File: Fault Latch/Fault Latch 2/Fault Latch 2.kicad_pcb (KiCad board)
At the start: 2 copper layers, 85 x 85 mm, 108 parts, among them J1 1053141312, J3 1053131202, J4 1053131202, K101 Fujitsu_FTR-LYAA005x, K102 Fujitsu_FTR-LYAA005x, K103 Fujitsu_FTR-LYAA005x, Q101 Q_NPN_BEC, Q102 Q_NPN_BEC, Q103 Q_NPN_BEC, Q104 Q_NPN_BEC, Q105 Q_NMOS_GSD, Q106 Q_NMOS_GSD, Q107 Q_PMOS_GSD, Q108 Q_PMOS_GSD, Q109 Q_PMOS_GSD, Q110 Q_NPN_BEC, Q111 Q_NPN_BEC, Q112 Q_NMOS_GSD, Q113 Q_NMOS_GSD, Q114 Q_NMOS_GSD, Q115 Q_NMOS_GSD, Q116 Q_NMOS_GSD, SW101 SW_Omron_B3FS, SW102 SW_Omron_B3FS, SW103 SW_Omron_B3FS, U101 SFH617A-1, U102 SFH617A-1, U103 SFH617A-1, U104 74AHC1G00, U105 74AHC1G00, U106 74AHC1G00, U107 74LS279, U109 SFH617A-1, U110 SFH617A-1, U117 74AHC1G00, U118 LM555xM, U119 74AHC1G00, U121 SFH617A-1, U2 LM1117DT-5.0

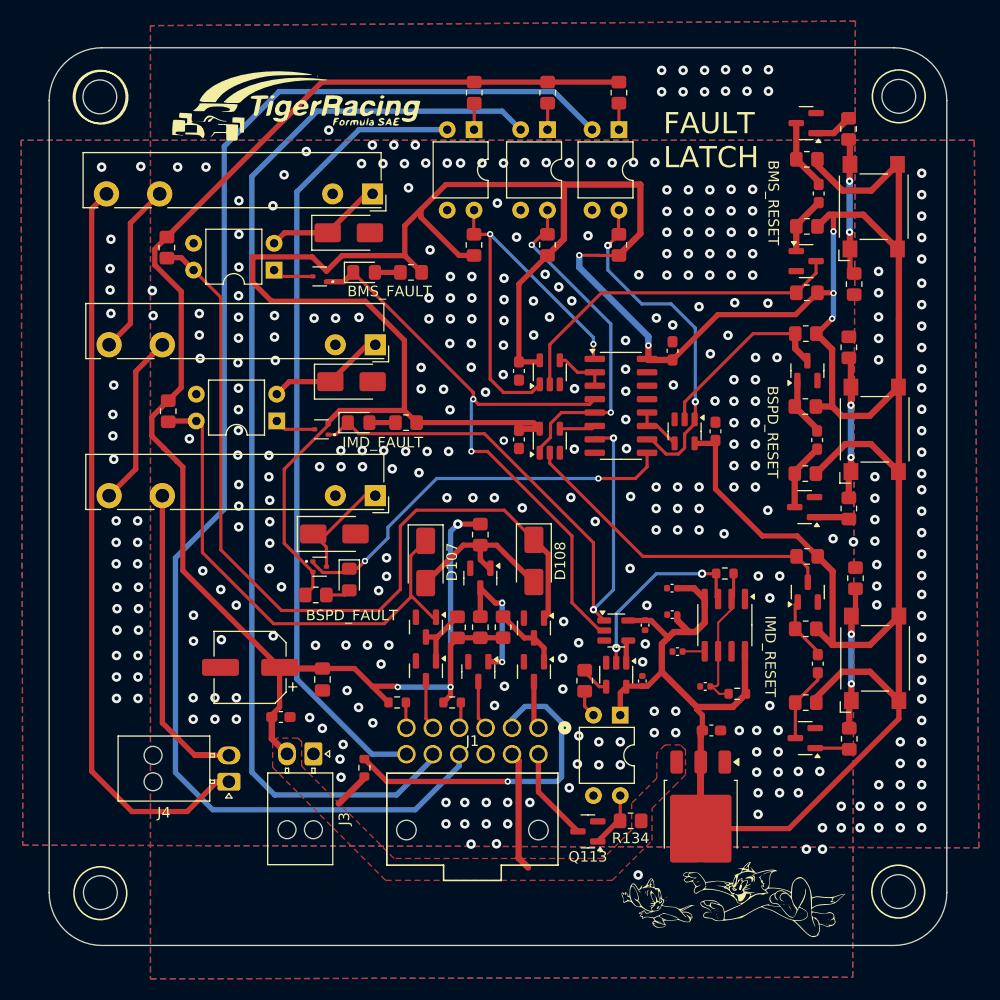
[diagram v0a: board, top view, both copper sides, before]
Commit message: Added Measuring points to Fault Latch
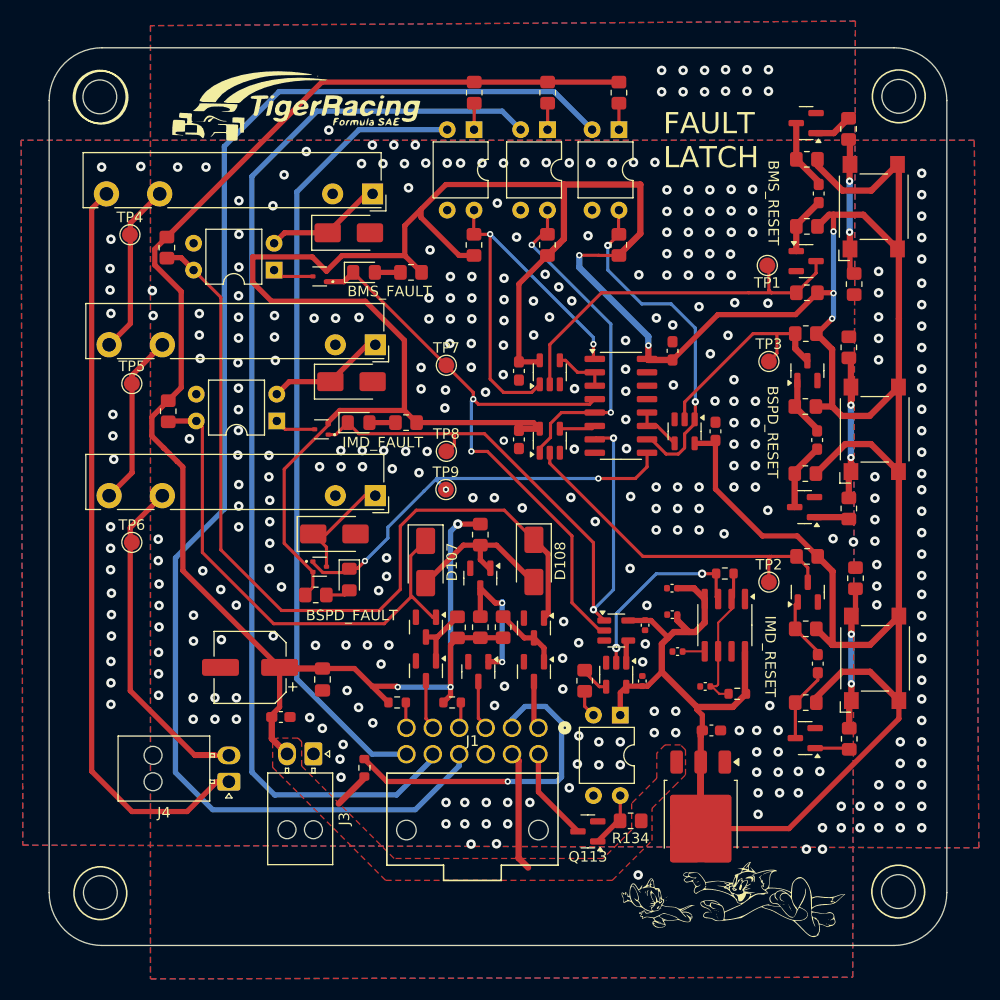
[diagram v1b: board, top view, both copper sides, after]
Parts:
- added TP1: TestPoint_BMS, TestPoint:TestPoint_Pad_D1.5mm, F.Cu at (137.3, 65.0)
- added TP2: TestPoint_IMD, TestPoint:TestPoint_Pad_D1.5mm, F.Cu at (137.4, 95.0)
- added TP3: TestPoint_BSPD, TestPoint:TestPoint_Pad_D1.5mm, F.Cu at (137.4, 74.1)
- added TP4: TestPoint_BMS_Shutdown, TestPoint:TestPoint_Pad_D1.5mm, F.Cu at (76.9, 62.1)
- added TP5: TestPoint_IMD_Shutdown, TestPoint:TestPoint_Pad_D1.5mm, F.Cu at (77.1, 76.2)
- added TP6: TestPoint_BSPD_Shutdown, TestPoint:TestPoint_Pad_D1.5mm, F.Cu at (77.1, 91.2)
- added TP7: TestPoint_SR_BMS, TestPoint:TestPoint_Pad_D1.5mm, F.Cu at (106.9, 74.4)
- added TP8: TestPoint_SR_IMD, TestPoint:TestPoint_Pad_D1.5mm, F.Cu at (106.9, 82.6)
- added TP9: TestPoint_SR_BSPD, TestPoint:TestPoint_Pad_D1.5mm, F.Cu at (106.9, 86.2)
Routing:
- net /NRESET_BSPD: track 17.8 -> 20.8 mm
- net /NRESET_BMS: track 32.9 -> 35.7 mm
- net /NRESET_IMD: track 30.9 -> 33.5 mm
- net /Shutdown Circuit Out: track 31.0 -> 33.5 mm
- net /IMD_SR: track 56.9 -> 58.9 mm
- net Net-(D103-K): track 38.2 -> 39.6 mm, vias 2 -> 3
- net GND: vias 355 -> 343

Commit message: Fault Latch Spring Semester
Fixed TSSI, Logic, and everything.
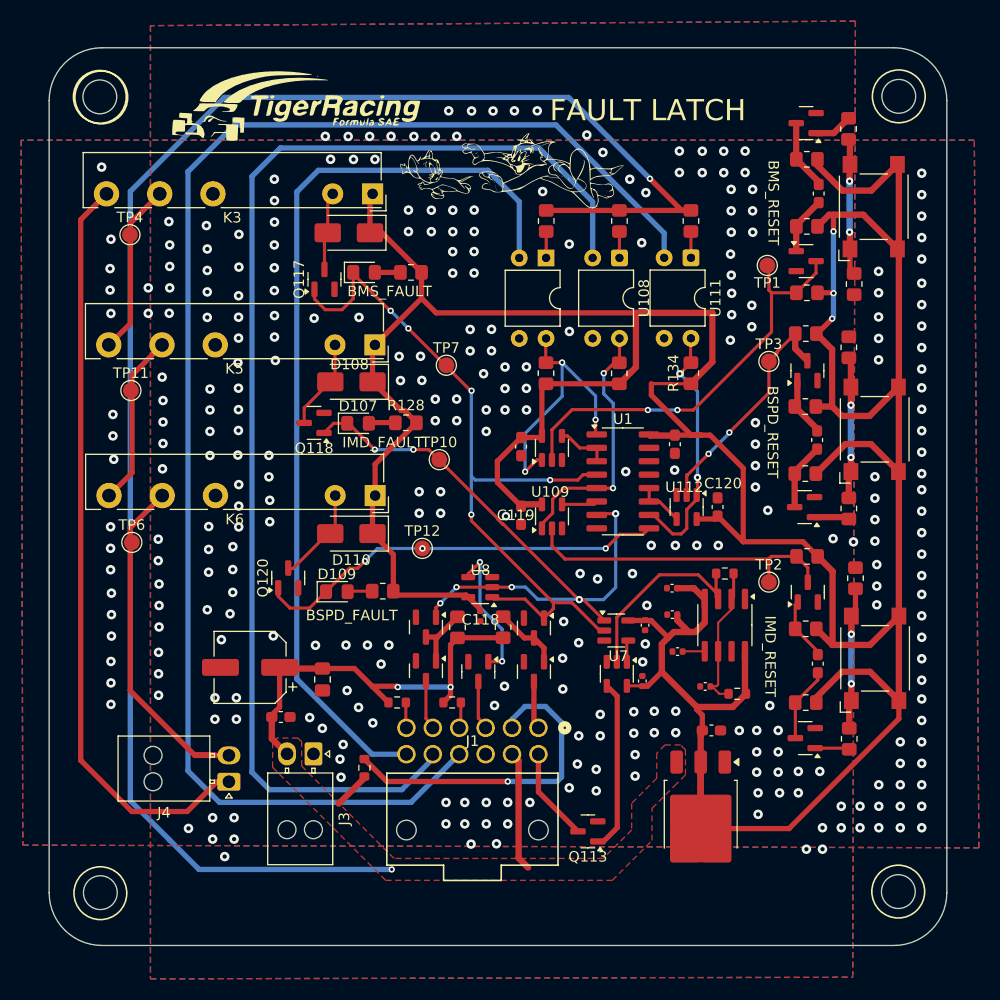
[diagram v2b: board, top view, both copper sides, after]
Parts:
- removed C103, C104: 100n, Capacitor_SMD:C_0603_1608Metric_Pad1.08x0.95mm_HandSolder
- removed D101, D103: RED, LED_SMD:LED_0805_2012Metric_Pad1.15x1.40mm_HandSolder
- removed D105, D106: D_Schottky, Diode_SMD:D_SMA
- removed K101, K102, K103: Fujitsu_FTR-LYAA005x, Relay_THT:Relay_SPST-NO_Fujitsu_FTR-LYAA005x_FormA_Vertical
- removed Q107, Q108, Q109: Q_PMOS_GSD, Package_TO_SOT_SMD:SOT-523
- removed Q116: Q_NMOS_GSD, Package_TO_SOT_SMD:SOT-23
- removed R103, R104: 220, Resistor_SMD:R_0805_2012Metric_Pad1.20x1.40mm_HandSolder
- removed R107, R109: 1k, Resistor_SMD:R_0805_2012Metric_Pad1.20x1.40mm_HandSolder
- removed R116, R118: 2k, Resistor_SMD:R_0805_2012Metric_Pad1.20x1.40mm_HandSolder
- removed R138: 10k, Resistor_SMD:R_0805_2012Metric_Pad1.20x1.40mm_HandSolder
- removed TP5: TestPoint_IMD_Shutdown, TestPoint:TestPoint_Pad_D1.5mm
- removed TP8: TestPoint_SR_IMD, TestPoint:TestPoint_Pad_D1.5mm
- removed TP9: TestPoint_SR_BSPD, TestPoint:TestPoint_Pad_D1.5mm
- removed U102, U103, U110, U121: SFH617A-1, Package_DIP:DIP-4_W7.62mm
- removed U105, U106, U119: 74AHC1G00, Package_TO_SOT_SMD:SOT-23-5
- removed U107: 74LS279, Package_SO:SOIC-16_3.9x9.9mm_P1.27mm
- added C118: 0.1u, Capacitor_SMD:C_0402_1005Metric, F.Cu at (110.1, 98.2)
- added C119: 100n, Capacitor_SMD:C_0603_1608Metric_Pad1.08x0.95mm_HandSolder, F.Cu at (114.0, 88.6)
- added C120: 100n, Capacitor_SMD:C_0603_1608Metric_Pad1.08x0.95mm_HandSolder, F.Cu at (132.6, 87.9)
- added D109: RED, LED_SMD:LED_0805_2012Metric_Pad1.15x1.40mm_HandSolder, F.Cu at (96.5, 95.9)
- added D110: D_Schottky, Diode_SMD:D_SMA, F.Cu at (97.9, 90.4)
- added K3: Fujitsu_FTR-LYCA005x, Relay_THT:Relay_SPDT_Fujitsu_FTR-LYCA005x_FormC_Vertical, F.Cu at (99.9, 58.2)
- added K5: Fujitsu_FTR-LYCA005x, Relay_THT:Relay_SPDT_Fujitsu_FTR-LYCA005x_FormC_Vertical, F.Cu at (100.1, 72.5)
- added K6: Fujitsu_FTR-LYCA005x, Relay_THT:Relay_SPDT_Fujitsu_FTR-LYCA005x_FormC_Vertical, F.Cu at (100.1, 86.8)
- added Q117: Q_NMOS_GSD, Package_TO_SOT_SMD:SOT-23, F.Cu at (95.4, 66.3)
- added Q118: Q_NMOS_GSD, Package_TO_SOT_SMD:SOT-23, F.Cu at (94.4, 79.9)
- added Q120: Q_NMOS_GSD, Package_TO_SOT_SMD:SOT-23, F.Cu at (91.9, 94.6)
- added R128: 2k, Resistor_SMD:R_0805_2012Metric_Pad1.20x1.40mm_HandSolder, F.Cu at (103.1, 79.9)
- added TP10: TestPoint_SR_IMD, TestPoint:TestPoint_Pad_D1.5mm, F.Cu at (106.2, 83.4)
- added TP11: TestPoint_IMD_Shutdown, TestPoint:TestPoint_Pad_D1.5mm, F.Cu at (77.0, 76.8)
- added TP12: TestPoint_SR_BSPD, TestPoint:TestPoint_Pad_D1.5mm, F.Cu at (104.6, 91.8)
- added U1: 74LS279, Package_SO:SOIC-16_3.9x9.9mm_P1.27mm, F.Cu at (123.6, 85.4)
- added U108: SFH617A-1, Package_DIP:DIP-4_W7.62mm, F.Cu at (123.3, 64.3)
- added U111: SFH617A-1, Package_DIP:DIP-4_W7.62mm, F.Cu at (130.1, 64.3)
- added U112: 74AHC1G00, Package_TO_SOT_SMD:SOT-23-5, F.Cu at (129.6, 87.9)
- added U7: SN74AHC1G08DBVR, Package_TO_SOT_SMD:SOT-23-5, F.Cu at (123.0, 103.7)
- added U8: SN74AHC1G08DBVR, Package_TO_SOT_SMD:SOT-23-5, F.Cu at (110.1, 95.4)
- D107: value D_Schottky -> RED; footprint Diode_SMD:D_SMA -> LED_SMD:LED_0805_2012Metric_Pad1.15x1.40mm_HandSolder
- R125: value 10k -> 220
- R126, R134: value 10k -> 1k
- R137: value 10k -> 2k
- U109: value SFH617A-1 -> 74AHC1G00; footprint Package_DIP:DIP-4_W7.62mm -> Package_TO_SOT_SMD:SOT-23-5
- moved G*** 72.1 mm to (112.3, 55.9)
- moved R133 44.7 mm to (130.1, 60.8)
- moved R125 42.9 mm to (123.3, 60.8), turned to 90 degrees
- moved R126 42.9 mm to (123.3, 75.2), turned to 90 degrees
- moved R134 42.8 mm to (130.1, 75.2), turned to 90 degrees
- moved U109 35.2 mm to (116.9, 88.7), turned to 90 degrees
- moved D108 24.2 mm to (97.9, 76.0), turned to 180 degrees
- moved D107 14.6 mm to (98.5, 79.9), turned to 0 degrees
- moved R102 13.9 mm to (116.4, 60.8)
- moved U101 13.9 mm to (116.3, 64.3)
- moved R106 13.9 mm to (116.3, 75.2)
- moved R137 10.7 mm to (100.9, 95.8), turned to 0 degrees
- moved C117 8.85 mm to (128.5, 81.9), turned to -90 degrees
- moved U104 7.16 mm to (116.9, 82.3)
- moved C102 7.16 mm to (114.0, 82.1)
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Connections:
- D104 pad 1: Net-(D104-K) -> +5V
- D104 pad 2: GND -> Net-(D104-A)
- D107 pad 1: /IMD_LED -> /IMD_SR
- D108 pad 1: /BMS_Green -> +5V
- D108 pad 2: Net-(D107-A) -> Net-(D108-A)
- Q105 pad 1: /IMD_LED -> /IMD_SR
- Q114 pad 1: /BMS_Green -> /BMS_SR
- R125 pad 1: +12V -> Net-(R125-Pad1)
- R125 pad 2: /BMS_Green -> +12V
- R126 pad 1: +12V -> +5V
- R126 pad 2: /IMD_LED -> /NIMD_LV
- R133 pad 2: Net-(R133-Pad2) -> +12V
- R134 pad 1: +12V -> +5V
- R134 pad 2: Net-(Q113-G) -> /NBPSD_LV
- R137 pad 1: +12V -> Net-(D109-A)
- R137 pad 2: Net-(D107-A) -> +5V
- U109 pad 1: Net-(Q107-D) -> /NIMD_LV
- U109 pad 2: Net-(D104-K) -> /NRESET_IMD
- U109 pad 4: /BMS_Green -> Net-(U1B-~{S})
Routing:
- net /BMS_Green: track 79.3 -> 0.00 mm
- net +5V: track 433.1 -> 380.7 mm, vias 5 -> 3
- net /IMD_LED: track 48.1 -> 0.00 mm
- net +12V: track 169.3 -> 213.9 mm, vias 3 -> 4
- net Net-(D103-K): track 39.6 -> 0.00 mm, vias 3 -> 0
- net Net-(D109-K): track 0.00 -> 39.5 mm, vias 0 -> 3
- net Net-(K5-Pad11): track 0.00 -> 16.4 mm
- net Net-(K102-Pad14): track 16.4 -> 0.00 mm
- net Net-(D107-A): track 15.8 -> 2.47 mm
- net /NBMS_LV: track 39.0 -> 25.9 mm, vias 2 -> 3
- net /BMS_SR: track 59.9 -> 72.4 mm, vias 2 -> 5
- net /NBMS_HV: track 76.1 -> 87.9 mm
- net Net-(D104-K): track 11.3 -> 0.00 mm
- net Net-(D106-K): track 11.3 -> 0.00 mm
- net /IMD_HV: track 105.0 -> 116.3 mm
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
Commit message: Changed Optocoupler to mosfet and added resistor to tssi red
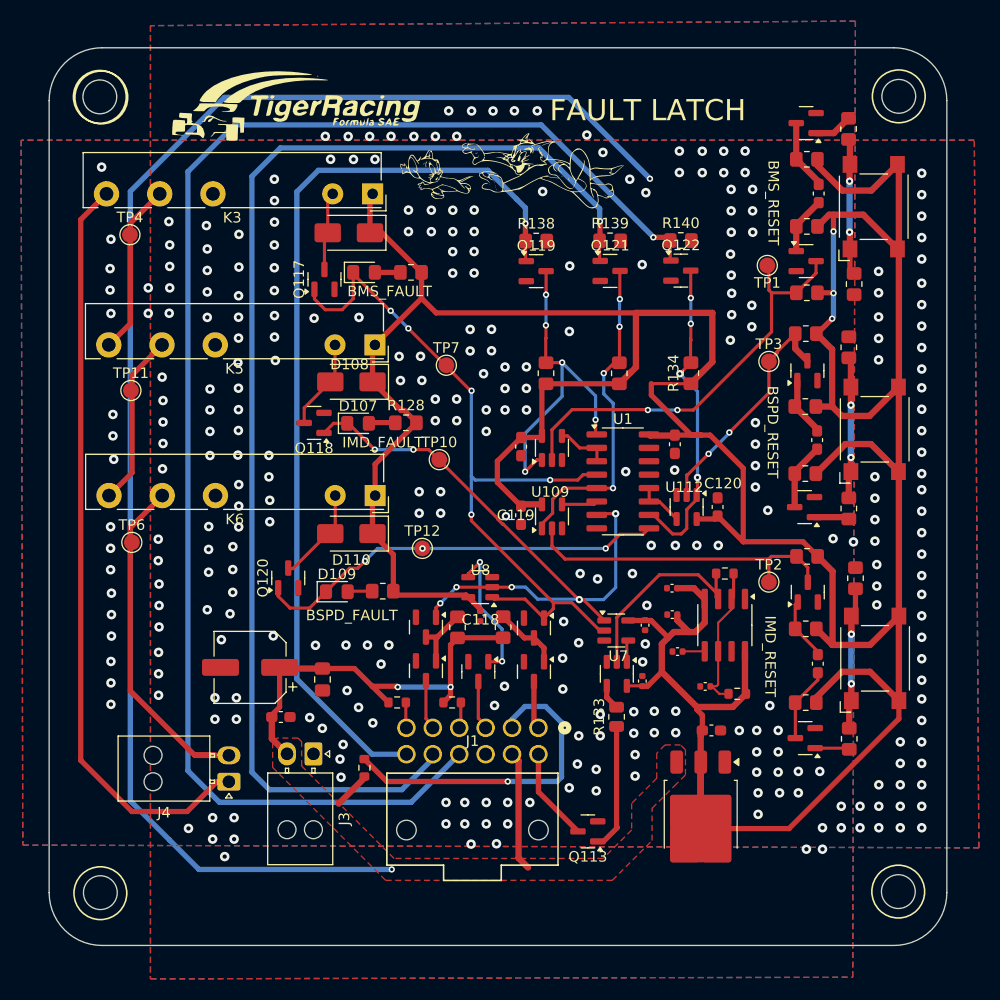
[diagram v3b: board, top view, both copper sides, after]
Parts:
- removed R102, R125: 220, Resistor_SMD:R_0805_2012Metric_Pad1.20x1.40mm_HandSolder
- removed U101, U108, U111: SFH617A-1, Package_DIP:DIP-4_W7.62mm
- added Q119: Q_NMOS_GSD, Package_TO_SOT_SMD:SOT-23, F.Cu at (115.4, 65.5)
- added Q121: Q_NMOS_GSD, Package_TO_SOT_SMD:SOT-23, F.Cu at (122.4, 65.5)
- added Q122: Q_NMOS_GSD, Package_TO_SOT_SMD:SOT-23, F.Cu at (129.1, 65.5)
- added R138: 10k, Resistor_SMD:R_0805_2012Metric_Pad1.20x1.40mm_HandSolder, F.Cu at (115.4, 62.7)
- added R139: 10k, Resistor_SMD:R_0805_2012Metric_Pad1.20x1.40mm_HandSolder, F.Cu at (122.4, 62.7)
- added R140: 10k, Resistor_SMD:R_0805_2012Metric_Pad1.20x1.40mm_HandSolder, F.Cu at (129.1, 62.6)
- R133: value 220 -> 680; footprint Resistor_SMD:R_0805_2012Metric_Pad1.20x1.40mm_HandSolder -> Resistor_SMD:R_0805_2012Metric
- TP10: value TestPoint_SR_IMD -> TestPoint_SR_BMS
- TP12: value TestPoint_SR_BSPD -> TestPoint_SR_BMS
- moved R133 47.5 mm to (123.0, 107.7)
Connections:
- R133 pad 1: Net-(R133-Pad1) -> Net-(Q113-G)
- R133 pad 2: +12V -> Net-(R133-Pad2)
- U7 pad 4: Net-(Q113-G) -> Net-(R133-Pad2)
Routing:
- net +12V: track 213.9 -> 195.0 mm
- net /NBPSD_LV: track 23.1 -> 29.7 mm, vias 2 -> 4
- net /NIMD_LV: track 23.9 -> 30.3 mm, vias 2 -> 4
- net /NBMS_LV: track 25.9 -> 32.3 mm, vias 3 -> 5
- net Net-(Q113-G): track 16.2 -> 12.0 mm
- net Net-(R133-Pad1): track 2.58 -> 0.00 mm
- net Net-(R125-Pad1): track 2.53 -> 0.00 mm
- net Net-(R102-Pad1): track 2.49 -> 0.00 mm
- net Net-(R133-Pad2): track 0.00 -> 2.40 mm
- net /IMD_HV: track 116.3 -> 117.0 mm, vias 0 -> 1
- net /NBMS_HV: track 87.9 -> 88.5 mm, vias 0 -> 1
- net /BSPD_HV: track 139.1 -> 139.5 mm, vias 0 -> 1

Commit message: Fault Latch V3
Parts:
- added J5: 1053131202, Connector_Molex:Molex_Nano-Fit_105313-xx02_1x02_P2.50mm_Horizontal, F.Cu at (84.2, 112.7)
- added Q123: Q_NMOS_GSD, Package_TO_SOT_SMD:SOT-23, F.Cu at (115.4, 61.4)
- added Q124: Q_NMOS_GSD, Package_TO_SOT_SMD:SOT-23, F.Cu at (122.5, 61.4)
- added Q125: Q_NMOS_GSD, Package_TO_SOT_SMD:SOT-23, F.Cu at (129.2, 61.4)
- added R107: 1k, Resistor_SMD:R_0805_2012Metric_Pad1.20x1.40mm_HandSolder, F.Cu at (119.2, 61.3)
- added R109: 1k, Resistor_SMD:R_0805_2012Metric_Pad1.20x1.40mm_HandSolder, F.Cu at (126.0, 61.3)
- added R116: 1k, Resistor_SMD:R_0805_2012Metric_Pad1.20x1.40mm_HandSolder, F.Cu at (132.4, 61.3)
- added U3: ~, Package_TO_SOT_SMD:SOT-223, F.Cu at (91.8, 113.7)
- moved G*** 69.2 mm to (107.3, 124.9)
- moved J4 17.3 mm to (86.0, 96.6)
- moved J3 11.5 mm to (84.4, 117.2)
- moved TP6 6.03 mm to (83.0, 90.0)
- moved R138 4.89 mm to (115.4, 57.8)
- moved R139 4.87 mm to (122.4, 57.8)
- moved R140 4.84 mm to (129.2, 57.8)
- moved C115 2.54 mm to (93.6, 106.9)
- moved R135 2.23 mm to (99.8, 114.7)
- moved C114 1.55 mm to (96.7, 104.2)
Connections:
- J3 pad 2: +12V -> /LVB
- Q119 pad 1: /NBMS_HV -> Net-(Q119-G)
- Q121 pad 1: /IMD_HV -> Net-(Q121-G)
- Q122 pad 1: /BSPD_HV -> Net-(Q122-G)
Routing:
- net /Shutdown Circuit Out: track 33.5 -> 9.79 mm
- net +12V: track 195.0 -> 216.1 mm
- net /Load Switch +: track 0.00 -> 19.5 mm
- net /Shutdown Circuit In: track 71.9 -> 53.4 mm
- net /Load Switch -: track 0.00 -> 12.2 mm
- net /LVB: track 0.00 -> 8.12 mm
- net /IMD_HV: track 117.0 -> 109.7 mm
- net /BSPD_HV: track 139.5 -> 133.0 mm
- net Net-(Q119-G): track 0.00 -> 6.36 mm
- net Net-(Q121-G): track 0.00 -> 6.11 mm
- net Net-(Q122-G): track 0.00 -> 5.92 mm
- net /NBMS_HV: track 88.5 -> 86.2 mm
- net /BMS Light In: track 31.5 -> 30.0 mm
- net GND: vias 313 -> 260
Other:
- board text added: "FAULT LATCH V3"
- board text removed: "FAULT LATCH"
